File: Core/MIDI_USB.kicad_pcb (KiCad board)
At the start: 4 copper layers, 37.8 x 99.8 mm, 114 parts, among them J1 Conn_01x04, J10 AudioJack3_SwitchTR, J4 Conn_01x06, J5 USB_C_Receptacle_USB2.0, J6 Conn_02x08_Odd_Even, J7 AudioJack3_SwitchTR, J8 AudioJack3_SwitchTR, J9 AudioJack3_SwitchTR, Q1 ZXMP3A13, Q2 PMV88ENER, Q3 MMBT3904, Q5 ZXMP3A13, Q6 MMBT3904, SW1 SW_Push_DPDT, SW2 SW_SPST, SW4 SW_SPST, U1 ATSAMD21G17D-A, U10 TLE9250V, U11 CAT250640VI, U12 APS1604M, U4 TL072, U5 MIC5504-3.3YM5, U6 ES9023P, U7 PCM1808, U8 TL072, U9 MCP2517FD-xSL, Y1 20MHz, Y2 32.768kHz

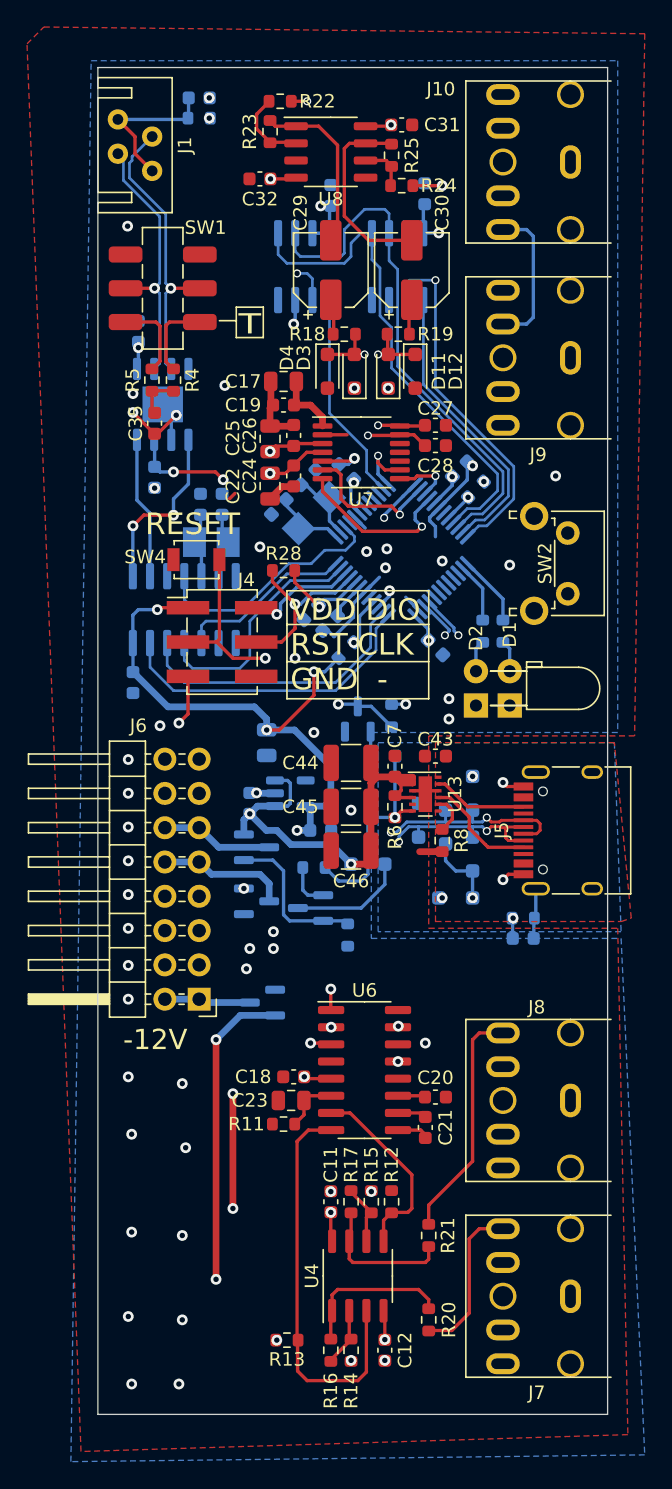
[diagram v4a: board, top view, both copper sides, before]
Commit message: Adjust vias
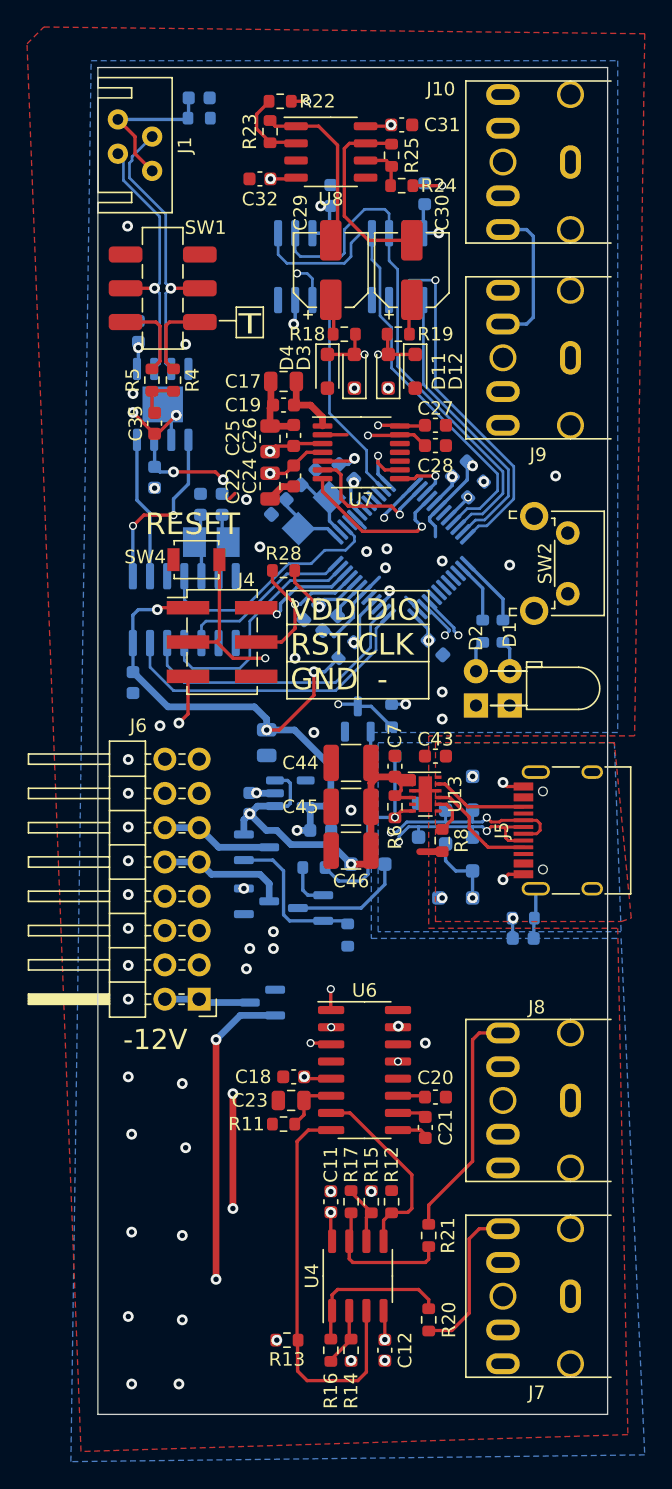
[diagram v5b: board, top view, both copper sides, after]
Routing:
- net GND: vias 56 -> 55
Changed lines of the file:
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@@
   (via (at 135.25 149) (size 0.8) (drill 0.4) (layers "F.Cu" "B.Cu") (free) (net 1))
   (via (at 158.5 126.8) (size 0.8) (drill 0.4) (layers "F.Cu" "B.Cu") (free) (net 1))
-  (via (at 141.25 94) (size 0.8) (drill 0.4) (layers "F.Cu" "B.Cu") (net 1))
+  (via (at 139.5 110.75) (size 0.8) (drill 0.4) (layers "F.Cu" "B.Cu") (free) (net 1))
   (via (at 144.25 155.5) (size 0.8) (drill 0.4) (layers "F.Cu" "B.Cu") (free) (net 1))
   (via (at 135.5 187.75) (size 0.8) (drill 0.4) (layers "F.Cu" "B.Cu") (free) (net 1))
-  (via (at 142.4 113.8) (size 0.8) (drill 0.4) (layers "F.Cu" "B.Cu") (net 1))
   (via (at 163 143.2) (size 0.8) (drill 0.4) (layers "F.Cu" "B.Cu") (net 1))
   (via (at 154.3 127.3) (size 0.8) (drill 0.4) (layers "F.Cu" "B.Cu") (free) (net 1))
@@
   (via (at 154.4 125.9) (size 0.8) (drill 0.4) (layers "F.Cu" "B.Cu") (free) (net 1))
   (via (at 135.25 141.5) (size 0.8) (drill 0.4) (layers "F.Cu" "B.Cu") (free) (net 1))
-  (via (at 141.25 92.5) (size 0.8) (drill 0.4) (layers "F.Cu" "B.Cu") (net 1))
   (via (at 152 119.2) (size 0.8) (drill 0.4) (layers "F.Cu" "B.Cu") (net 1))
   (via (at 144 157) (size 0.8) (drill 0.4) (layers "F.Cu" "B.Cu") (free) (net 1))
@@
   (via (at 139.5 170.25) (size 0.8) (drill 0.4) (layers "F.Cu" "B.Cu") (free) (net 1))
   (via (at 145 125.75) (size 0.8) (drill 0.4) (layers "F.Cu" "B.Cu") (free) (net 1))
-  (via (at 159 138.5) (size 0.8) (drill 0.4) (layers "F.Cu" "B.Cu") (net 1))
+  (via (at 158.5 138.5) (size 0.8) (drill 0.4) (layers "F.Cu" "B.Cu") (net 1))
   (via (at 166.9 120.5) (size 0.8) (drill 0.4) (layers "F.Cu" "B.Cu") (free) (net 1))
   (via (at 163.5 127.1) (size 0.8) (drill 0.4) (layers "F.Cu" "B.Cu") (free) (net 1))
   (via (at 144.75 143.975) (size 0.8) (drill 0.4) (layers "F.Cu" "B.Cu") (net 1))
   (via (at 163 150.4) (size 0.8) (drill 0.4) (layers "F.Cu" "B.Cu") (net 1))
-  (via (at 159 137) (size 0.8) (drill 0.4) (layers "F.Cu" "B.Cu") (net 1))
+  (via (at 158.5 136.5) (size 0.8) (drill 0.4) (layers "F.Cu" "B.Cu") (net 1))
   (via (at 147.6 134) (size 0.8) (drill 0.4) (layers "F.Cu" "B.Cu") (free) (net 1))
   (via (at 135.25 144) (size 0.8) (drill 0.4) (layers "F.Cu" "B.Cu") (free) (net 1))
   (via (at 150.25 173.5) (size 0.8) (drill 0.4) (layers "F.Cu" "B.Cu") (net 1))
+  (via (at 144 122.25) (size 0.8) (drill 0.4) (layers "F.Cu" "B.Cu") (free) (net 1))
   (via (at 139 187.75) (size 0.8) (drill 0.4) (layers "F.Cu" "B.Cu") (free) (net 1))
   (via (at 135.25 151.5) (size 0.8) (drill 0.4) (layers "F.Cu" "B.Cu") (free) (net 1))
@@
   (segment (start 145.74 130.26) (end 144.725 130.26) (width 0.25) (layer "F.Cu") (net 25))
   (segment (start 146.25 130.75) (end 146.23 130.75) (width 0.25) (layer "F.Cu") (net 25))
-  (via (at 146.25 130.75) (size 0.8) (drill 0.4) (layers "F.Cu" "B.Cu") (net 25))
+  (via (at 146.25 130.75) (size 0.6) (drill 0.4) (layers "F.Cu" "B.Cu") (net 25))
   (segment (start 146.525 130.475) (end 146.525 129.949695) (width 0.25) (layer "B.Cu") (net 25))
   (segment (start 146.25 130.75) (end 146.525 130.475) (width 0.25) (layer "B.Cu") (net 25))
@@
   (segment (start 147.6 131.8) (end 146.6 132.8) (width 0.25) (layer "F.Cu") (net 26))
   (segment (start 147.6 130) (end 147.6 131.8) (width 0.25) (layer "F.Cu") (net 26))
-  (via (at 147.6 130) (size 0.8) (drill 0.4) (layers "F.Cu" "B.Cu") (net 26))
+  (via (at 147.6 130) (size 0.6) (drill 0.4) (layers "F.Cu" "B.Cu") (net 26))
   (segment (start 148 130) (end 148.836473 129.163527) (width 0.25) (layer "B.Cu") (net 26))
   (segment (start 148.836473 129.163527) (end 150.568706 129.163527) (width 0.25) (layer "B.Cu") (net 26))
@@
   (segment (start 143 134) (end 145.4 134) (width 0.25) (layer "F.Cu") (net 27))
   (segment (start 141.8 132.8) (end 143 134) (width 0.25) (layer "F.Cu") (net 27))
-  (via (at 145.4 134) (size 0.8) (drill 0.4) (layers "F.Cu" "B.Cu") (net 27))
+  (via (at 145.4 134) (size 0.6) (drill 0.4) (layers "F.Cu" "B.Cu") (net 27))
   (via (at 151.956847 132.843153) (size 0.8) (drill 0.4) (layers "F.Cu" "B.Cu") (net 27))
   (segment (start 145.4 133.4) (end 146 132.8) (width 0.25) (layer "In1.Cu") (net 27))
@@
   (segment (start 157.5 175.9625) (end 157.5 174.5) (width 0.25) (layer "F.Cu") (net 29))
   (segment (start 156.325 99) (end 158.5 99) (width 0.25) (layer "F.Cu") (net 30))
-  (via (at 158.5 99) (size 0.8) (drill 0.4) (layers "F.Cu" "B.Cu") (net 30))
+  (via (at 158.5 99) (size 0.6) (drill 0.4) (layers "F.Cu" "B.Cu") (net 30))
   (segment (start 161 106.75) (end 159.75 105.5) (width 0.25) (layer "In1.Cu") (net 30))
   (segment (start 163 106.75) (end 161 106.75) (width 0.25) (layer "In1.Cu") (net 30))
@@
   (segment (start 156.3 145.315) (end 155.4725 145.315) (width 0.25) (layer "F.Cu") (net 32))
   (segment (start 155.4725 145.315) (end 155 145.7875) (width 0.25) (layer "F.Cu") (net 32))
-  (via (at 155 145.7875) (size 0.8) (drill 0.4) (layers "F.Cu" "B.Cu") (net 32))
+  (via (at 155 145.7875) (size 0.6) (drill 0.4) (layers "F.Cu" "B.Cu") (net 32))
   (segment (start 150.825 150.5) (end 152.5 150.5) (width 0.25) (layer "B.Cu") (net 32))
   (segment (start 155 145.7875) (end 155 141.325) (width 0.25) (layer "B.Cu") (net 32))
@@
   (segment (start 152.6 124.6) (end 149.6375 121.6375) (width 0.25) (layer "F.Cu") (net 45))
   (segment (start 149.6375 121.6375) (end 149.6375 120.7) (width 0.25) (layer "F.Cu") (net 45))
-  (via (at 150.275 161.325) (size 0.8) (drill 0.4) (layers "F.Cu" "B.Cu") (net 45))
+  (via (at 150.275 161.325) (size 0.6) (drill 0.4) (layers "F.Cu" "B.Cu") (net 45))
   (via (at 157 124.25) (size 0.6) (drill 0.4) (layers "F.Cu" "B.Cu") (net 45))
   (segment (start 156.95 132.213604) (end 155.95 133.213604) (width 0.25) (layer "In2.Cu") (net 45))
@@
   (segment (start 156.45 120.7) (end 156.65 120.5) (width 0.25) (layer "F.Cu") (net 46))
   (segment (start 156.65 120.5) (end 158 120.5) (width 0.25) (layer "F.Cu") (net 46))
-  (via (at 150.25 158.5) (size 0.8) (drill 0.4) (layers "F.Cu" "B.Cu") (net 46))
+  (via (at 150.25 158.5) (size 0.6) (drill 0.4) (layers "F.Cu" "B.Cu") (net 46))
   (via (at 158 120.5) (size 0.6) (drill 0.4) (layers "F.Cu" "B.Cu") (net 46))
   (segment (start 150.25 158.5) (end 150.25 144.5) (width 0.25) (layer "In2.Cu") (net 46))
@@
   (segment (start 151 120.4) (end 150.65 120.05) (width 0.25) (layer "F.Cu") (net 47))
   (via (at 155.362701 123.362701) (size 0.6) (drill 0.4) (layers "F.Cu" "B.Cu") (net 47))
-  (via (at 155.225 163.865) (size 0.8) (drill 0.4) (layers "F.Cu" "B.Cu") (net 47))
+  (via (at 155.225 163.865) (size 0.6) (drill 0.4) (layers "F.Cu" "B.Cu") (net 47))
   (segment (start 149.75 144.25) (end 149.75 151.25) (width 0.25) (layer "In2.Cu") (net 47))
   (segment (start 155.95 131.940812) (end 155.05 132.840812) (width 0.25) (layer "In2.Cu") (net 47))
@@
   (segment (start 150.18 162.5) (end 150.275 162.595) (width 0.25) (layer "F.Cu") (net 48))
   (segment (start 148.75 162.5) (end 150.18 162.5) (width 0.25) (layer "F.Cu") (net 48))
-  (via (at 148.75 162.5) (size 0.8) (drill 0.4) (layers "F.Cu" "B.Cu") (net 48))
+  (via (at 148.75 162.5) (size 0.6) (drill 0.4) (layers "F.Cu" "B.Cu") (net 48))
   (via (at 154.2 123.6) (size 0.6) (drill 0.4) (layers "F.Cu" "B.Cu") (net 48))
   (segment (start 149 162.25) (end 148.75 162.5) (width 0.25) (layer "In2.Cu") (net 48))
@@
   (segment (start 150.155 115.855) (end 150.155 107.475) (width 0.2) (layer "B.Cu") (net 70))
   (segment (start 152.9 120.218019) (end 152.9 118.6) (width 0.2) (layer "B.Cu") (net 70))
-  (via (at 160.416637 122.083363) (size 0.8) (drill 0.4) (layers "F.Cu" "B.Cu") (net 71))
+  (via (at 160.416637 122.083363) (size 0.6) (drill 0.4) (layers "F.Cu" "B.Cu") (net 71))
   (segment (start 167.8 124.725) (end 166.750001 125.774999) (width 0.25) (layer "In1.Cu") (net 71))
   (segment (start 166.750001 125.774999) (end 164.358273 125.774999) (width 0.25) (layer "In1.Cu") (net 71))
@@
   (segment (start 160.416637 122.144024) (end 160.416637 122.083363) (width 0.25) (layer "B.Cu") (net 71))
   (via (at 154.6 129) (size 0.8) (drill 0.4) (layers "F.Cu" "B.Cu") (net 84))
-  (via (at 150.803237 137.402158) (size 0.8) (drill 0.4) (layers "F.Cu" "B.Cu") (net 84))
+  (via (at 150.803237 137.402158) (size 0.6) (drill 0.4) (layers "F.Cu" "B.Cu") (net 84))
   (segment (start 154.6 131.6) (end 154.6 129) (width 0.25) (layer "In2.Cu") (net 84))
   (segment (start 151.6 136.605395) (end 150.803237 137.402158) (width 0.25) (layer "In2.Cu") (net 84))
@@
   (segment (start 135.6 124.2) (end 136.4 123.4) (width 0.25) (layer "F.Cu") (net 115))
   (segment (start 136.4 123.4) (end 138.6 123.4) (width 0.25) (layer "F.Cu") (net 115))
-  (via (at 138.6 123.4) (size 0.8) (drill 0.4) (layers "F.Cu" "B.Cu") (net 115))
-  (via (at 135.6 124.2) (size 0.8) (drill 0.4) (layers "F.Cu" "B.Cu") (net 115))
+  (via (at 138.6 123.4) (size 0.6) (drill 0.4) (layers "F.Cu" "B.Cu") (net 115))
+  (via (at 135.6 124.2) (size 0.6) (drill 0.4) (layers "F.Cu" "B.Cu") (net 115))
   (segment (start 138.6 123.4) (end 138.6 122.2) (width 0.25) (layer "B.Cu") (net 115))
   (segment (start 135.59 124.21) (end 135.6 124.2) (width 0.25) (layer "B.Cu") (net 115))

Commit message: Switch to RP2040
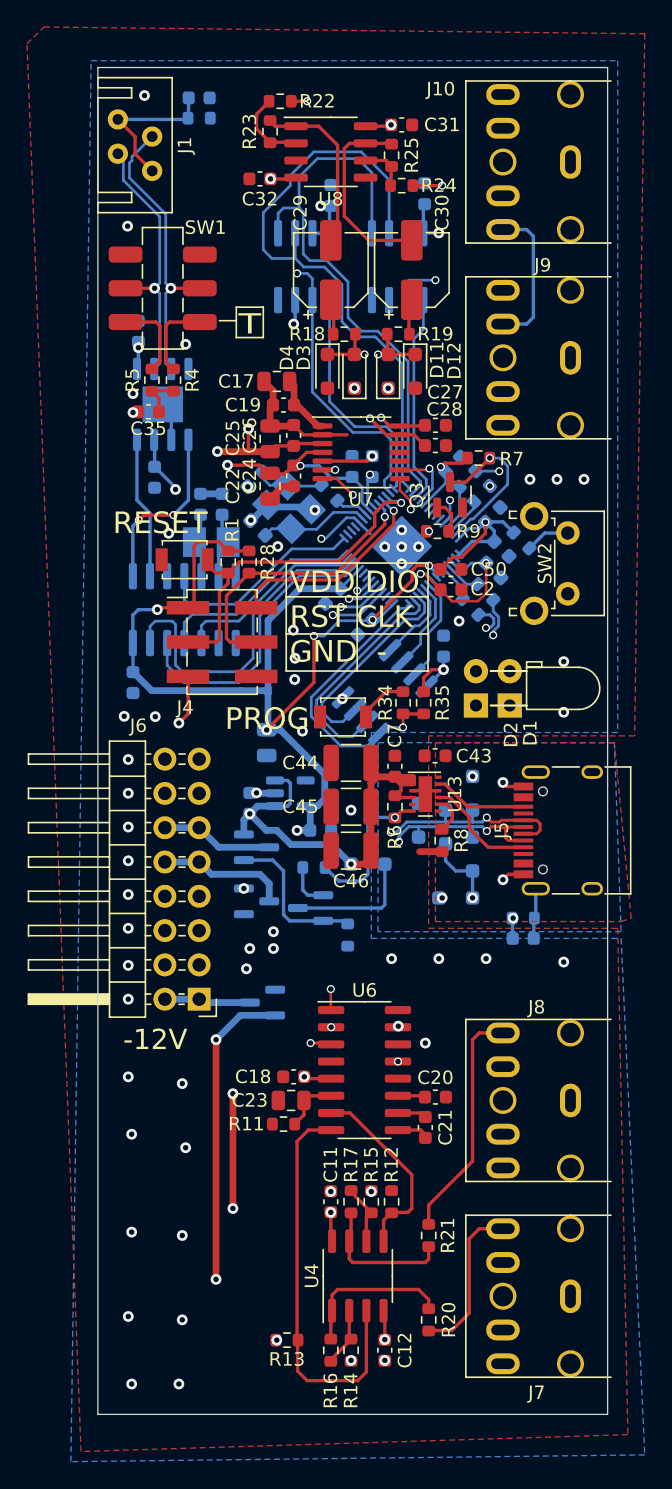
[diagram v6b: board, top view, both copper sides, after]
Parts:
- removed C3: 100nF, Capacitor_SMD:C_0603_1608Metric
- added C13: 100nF, Capacitor_SMD:C_0603_1608Metric, B.Cu at (152.8, 131.7)
- added C47: 100nF, Capacitor_SMD:C_0603_1608Metric, B.Cu at (151.8, 119.8)
- added C48: 100nF, Capacitor_SMD:C_0603_1608Metric, B.Cu at (159.3, 119.7)
- added C49: 100nF, Capacitor_SMD:C_0603_1608Metric, B.Cu at (162.2, 123.4)
- added C50: 100nF, Capacitor_SMD:C_0603_1608Metric, F.Cu at (159.2, 127.4)
- added C8: 100nF, Capacitor_SMD:C_0603_1608Metric, B.Cu at (158.6, 133.1)
- added C9: 100nF, Capacitor_SMD:C_0603_1608Metric, B.Cu at (150.4, 129.4)
- added R27: 1k, Resistor_SMD:R_0603_1608Metric, B.Cu at (150.2, 121.8)
- added R33: 27.4, Resistor_SMD:R_0603_1608Metric, B.Cu at (161.7, 129.1)
- added R34: 1k, Resistor_SMD:R_0603_1608Metric, F.Cu at (155.6, 137.3)
- added R35: NC, Resistor_SMD:R_0603_1608Metric, F.Cu at (157.1, 137.3)
- added SW3: SW_SPST, Button_Switch_SMD:SW_SPST_B3U-1000P, F.Cu at (151.2, 138.3)
- added U2: IS25LP032D, Package_SO:SOIC-8_3.9x4.9mm_P1.27mm, B.Cu at (154.2, 136.5)
- added locked: 27.4, Resistor_SMD:R_0603_1608Metric, B.Cu at (160.6, 130.2)
- C2, Q3, R7, R9: moved to F.Cu
- C4: value 100nF -> 1µF
- C41, C42: value 15pF -> 27pF
- R1: value 10k -> NC; moved to F.Cu
- R29: value 1M -> 100k
- U1: value ATSAMD21G17D-A -> RP2040; footprint Package_QFP:TQFP-48_7x7mm_P0.5mm -> Package_DFN_QFN:QFN-56-1EP_7x7mm_P0.4mm_EP3.2x3.2mm
- Y2: value 32.768kHz -> ECS-120-18-33-JGN-TR3; footprint Crystal:Crystal_SMD_EuroQuartz_EQ161-2Pin_3.2x1.5mm_HandSoldering -> Custom_FP:Crystal_SMD_3225-4Pin_3.2x2.5mm_HandSoldering
- moved R7 20.1 mm to (161.2, 119.2), turned to 0 degrees
- moved Q3 17.9 mm to (159.1, 121.9)
- moved R9 17.1 mm to (158.2, 124.6), turned to 180 degrees
- moved C5 13.8 mm to (162.9, 125.9), turned to -45 degrees
- moved C1 11.7 mm to (153.3, 119.8), turned to 90 degrees
- moved R2 11.6 mm to (160.4, 120.7), turned to 45 degrees
- moved R1 10.9 mm to (142.7, 126.9), turned to -90 degrees
- moved R3 10.2 mm to (161.4, 121.8), turned to 45 degrees
- moved C2 8.95 mm to (159.2, 128.9), turned to 0 degrees
- moved C4 7.14 mm to (162.3, 127.5)
- moved C41 5.30 mm to (144.8, 124.3), turned to 135 degrees
- moved R26 5.06 mm to (164.4, 125.3), turned to -45 degrees
- moved C42 2.70 mm to (144.7, 120.8)
- moved R28 2.63 mm to (144.2, 126.9), turned to -90 degrees
- moved Y2 1.90 mm to (147.2, 122.8), turned to -45 degrees
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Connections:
- C1 pad 1: +3V3 -> Net-(U1-VREG_VOUT)
- C2 pad 1: +3V3 -> Net-(U1-VREG_VOUT)
- C4 pad 1: +3V3 -> Net-(U1-VREG_VOUT)
- C41 pad 1: Net-(U1-PA01) -> Net-(U1-XIN)
- C42 pad 1: Net-(U1-PA00) -> Net-(C42-Pad1)
- C5 pad 1: Net-(U1-VDDCORE) -> +3V3
- U1 pad 1: Net-(U1-PA00) -> +3V3
- U1 pad 10: unconnected-(U1-PA05-Pad10) -> +3V3
- U1 pad 11: EEPROM_SS -> SPI_MISO
- U1 pad 12: I2S_DI -> CAN_SS
- U1 pad 13: I2S_DO -> SPI_SCK
- U1 pad 14: I2S_MCK -> SPI_MOSI
- U1 pad 15: I2S_SCK -> CAN_INT
- U1 pad 16: I2S_FS -> unconnected-(U1-GPIO13-Pad16)
- U1 pad 17: +3V3 -> unconnected-(U1-GPIO14-Pad17)
- U1 pad 18: GND -> unconnected-(U1-GPIO15-Pad18)
- U1 pad 19: unconnected-(U1-PB10-Pad19) -> GND
- U1 pad 2: Net-(U1-PA01) -> unconnected-(U1-GPIO0-Pad2)
- U1 pad 20: IO_BUTT -> Net-(U1-XIN)
- U1 pad 21: SPI2_MOSI -> Net-(U1-XOUT)
- U1 pad 22: SPI2_SCK -> +3V3
- U1 pad 23: RAM_SS -> Net-(U1-VREG_VOUT)
- U1 pad 24: SPI2_MISO -> SWCLK
- U1 pad 25: LED1 -> SWDIO
- U1 pad 26: LED2 -> RST
- U1 pad 27: unconnected-(U1-PA18-Pad27) -> SPI2_MISO
- U1 pad 28: unconnected-(U1-PA19-Pad28) -> EEPROM_SS
- U1 pad 29: unconnected-(U1-PA20-Pad29) -> SPI2_SCK
- U1 pad 3: CAN_INT -> unconnected-(U1-GPIO1-Pad3)
- U1 pad 30: unconnected-(U1-PA21-Pad30) -> SPI2_MOSI
- U1 pad 31: unconnected-(U1-PA22-Pad31) -> RAM_SS
- U1 pad 32: unconnected-(U1-PA23-Pad32) -> I2S_DI
- U1 pad 33: USB_D- -> +3V3
- U1 pad 34: USB_D+ -> unconnected-(U1-GPIO22-Pad34)
- U1 pad 35: GND -> unconnected-(U1-GPIO23-Pad35)
- U1 pad 36: +3V3 -> unconnected-(U1-GPIO24-Pad36)
- U1 pad 37: CAN_SS -> unconnected-(U1-GPIO25-Pad37)
- U1 pad 38: SPI_MISO -> IO_BUTT
- U1 pad 39: Net-(Q3-C) -> LED1
- U1 pad 4: unconnected-(U1-PA03-Pad4) -> I2S_DO
- U1 pad 40: RST -> LED2
- U1 pad 41: PROG -> Net-(Q3-C)
- U1 pad 42: GND -> +3V3
- U1 pad 43: Net-(U1-VDDCORE) -> +3V3
- U1 pad 45: SWCLK -> Net-(U1-VREG_VOUT)
- U1 pad 46: SWDIO -> /MCU_USB_D-
- U1 pad 47: SPI_MOSI -> /MCU_USB_D+
- U1 pad 48: SPI_SCK -> +3V3
- U1 pad 5: GND -> I2S_MCK
- U1 pad 6: +3V3 -> I2S_BCK
- U1 pad 7: unconnected-(U1-PB08-Pad7) -> I2S_FS
- U6 pad 1: I2S_SCK -> I2S_BCK
- U7 pad 8: I2S_SCK -> I2S_BCK
- Y2 pad 1: Net-(U1-PA01) -> Net-(C42-Pad1)
- Y2 pad 2: Net-(U1-PA00) -> GND
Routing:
- net I2S_BCK: track 0.00 -> 51.6 mm, vias 0 -> 3
- net +3V3: track 234.7 -> 283.7 mm
- net I2S_SCK: track 47.1 -> 0.00 mm, vias 2 -> 0
- net Net-(U1-VREG_VOUT): track 0.00 -> 25.2 mm, vias 0 -> 3
- net FLASH_CS: track 0.00 -> 22.4 mm, vias 0 -> 1
- net USB_ID: track 15.8 -> 35.8 mm, vias 1 -> 2
- net FLASH_SD1: track 0.00 -> 17.2 mm
- net Net-(D1-A): track 2.38 -> 18.9 mm, vias 0 -> 1
- net FLASH_SD2: track 0.00 -> 15.6 mm
- net Net-(D2-A): track 2.38 -> 16.7 mm, vias 0 -> 1
- net Net-(U1-XIN): track 0.00 -> 8.19 mm
- net SWCLK: track 13.0 -> 21.1 mm
- net FLASH_SD3: track 0.00 -> 7.82 mm
- net I2S_DO: track 47.3 -> 39.8 mm
- net SWDIO: track 8.18 -> 15.6 mm
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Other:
- board text added: "M2IDI_USB V2.0 GuavTek"
- board text added: "PROG"
- board text removed: "M2IDI_USB V1.1 GuavTek"

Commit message: Update metadata
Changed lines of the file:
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@@
   )
   (paper "A4")
+  (title_block
+    (title "M2IDI - USB CORE")
+    (date "2023-06-18")
+    (rev "2.0")
+    (company "GuavTek")
+  )
   (layers
     (0 "F.Cu" signal)
@@
     (property "ki_keywords" "cap capacitor")
     (attr smd)
-    (fp_text reference "C46" (at 0 -2.25) (layer "F.SilkS")
+    (fp_text reference "C46" (at 3.75 0) (layer "F.SilkS")
         (effects (font (size 1 1) (thickness 0.15)))
     )
@@
     (effects (font (size 1.6 1.6) (thickness 0.15)) (justify left bottom))
   )
-  (gr_text "VDD DIO\nRST CLK\nGND  - " (at 147.2 134.45) (layer "F.SilkS")
-    (effects (font (size 1.6 1.6) (thickness 0.2)) (justify left bottom))
+  (gr_text "VDD DIO\nRST CLK\nGND  - " (at 152.2 130.95) (layer "F.SilkS")
+    (effects (font (size 1.6 1.6) (thickness 0.2)))
   )
   (gr_text "-12V" (at 137.25 162.25) (layer "F.SilkS")
